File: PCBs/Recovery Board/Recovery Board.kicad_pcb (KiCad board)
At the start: 2 copper layers, 84.3 x 50.8 mm, 30 parts, among them J1 Conn_01x02, J2 Conn_01x02, J3 Conn_01x02, J4 Conn_01x02, J5 Conn_01x02, J6 Conn_01x02, U1 R-78E3.3-0.5, U2 PI4ULS5V201TAEX, U3 PI4ULS5V201TAEX, X1 XBee-S2C

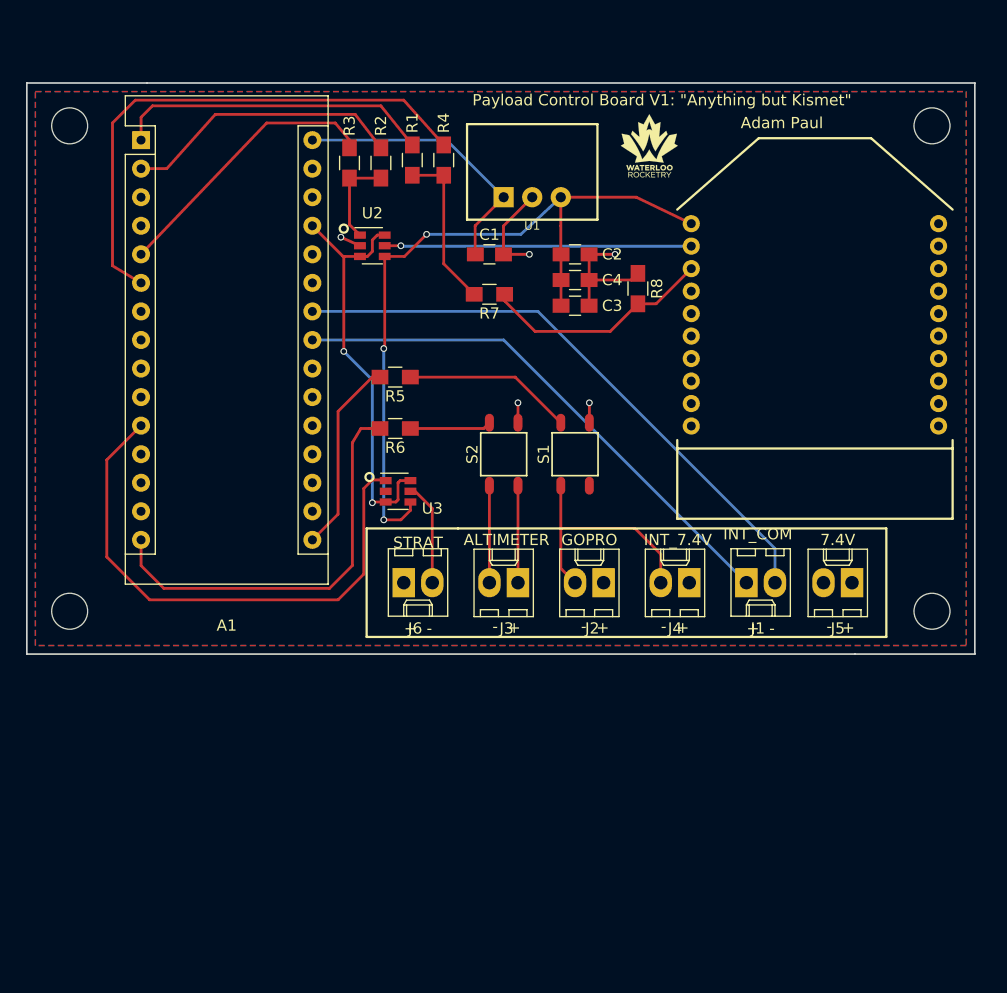
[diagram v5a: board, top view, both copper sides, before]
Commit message: swapped all mounting holes with plated ones, fixed disconnected components on recovery, added the 4 decoupling caps to recovery, fixed silk screen on pads in instr, fixed traces connecting through pads on recovery and instr, moved q1 on instr, brought trace in near u2 on instr, switched u2 & u3 to hand solder on instr, fixed xbee screen on recovery, fixed connector labels on recovery, removed recovery dims past edge cuts, fixed pad mask clearance on recovery
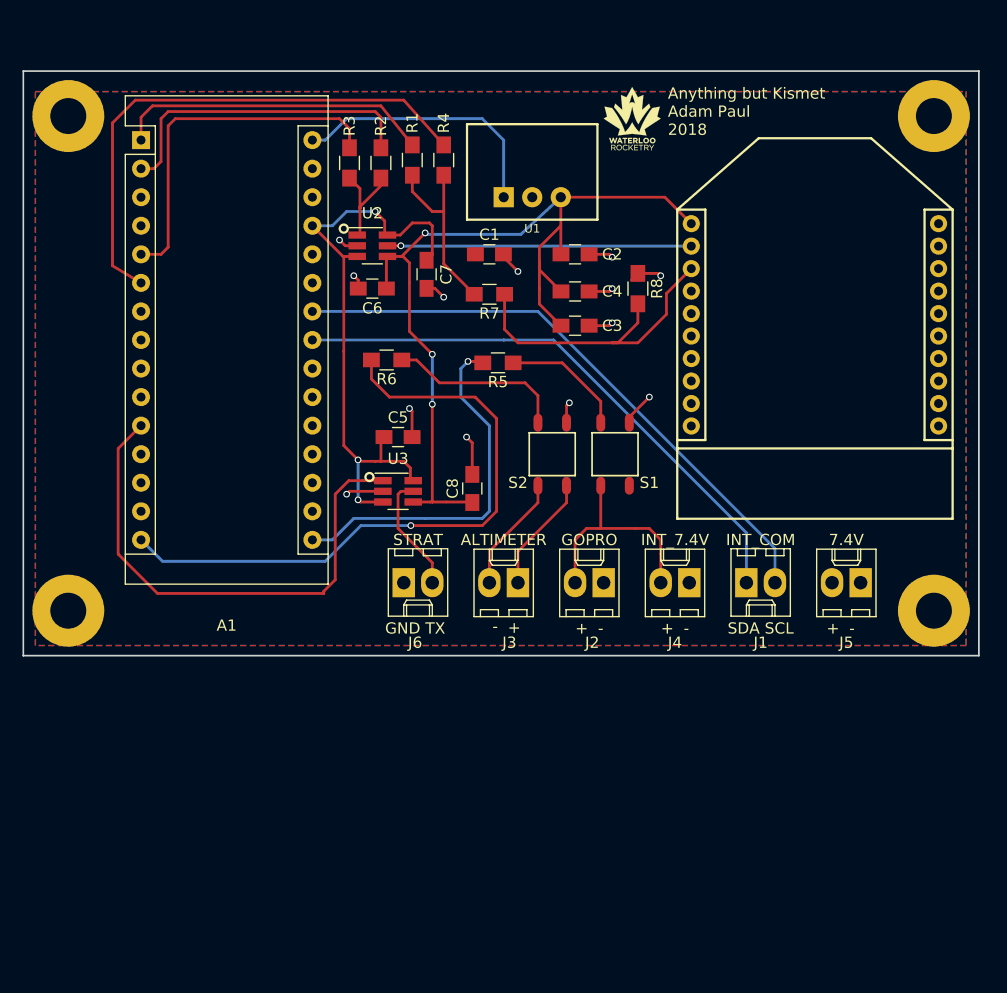
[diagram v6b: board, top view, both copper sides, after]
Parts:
- removed the REF** at (163.8, 146.1)
- removed the REF** at (87.1, 102.9)
- removed the REF** at (87.1, 146.1)
- added C5: 0.1uF, Capacitors_SMD:C_0805_HandSoldering, F.Cu at (116.3, 130.6)
- added C6: 0.1uF, Capacitors_SMD:C_0805_HandSoldering, F.Cu at (114.0, 117.3)
- added C7: 0.1uF, Capacitors_SMD:C_0805_HandSoldering, F.Cu at (118.9, 116.1)
- added C8: 0.1uF, Capacitors_SMD:C_0805_HandSoldering, F.Cu at (122.9, 135.1)
- added REF**: MountingHole_3.2mm_M3, Mounting_Holes:MountingHole_3.2mm_M3_Pad, F.Cu at (87.0, 102.0)
- added REF**: MountingHole_3.2mm_M3, Mounting_Holes:MountingHole_3.2mm_M3_Pad, F.Cu at (87.0, 146.0)
- added REF**: MountingHole_3.2mm_M3, Mounting_Holes:MountingHole_3.2mm_M3_Pad, F.Cu at (164.0, 146.0)
- REF**: footprint Mounting_Holes:MountingHole_3.2mm_M3 -> Mounting_Holes:MountingHole_3.2mm_M3_Pad
- U2, U3: value PI4ULS5V201TAEX -> PI4ULS5V201TAEX-RESCUE-instrumentation_board; footprint sot:SOT-23-6 -> TO_SOT_Packages_SMD:SOT-23-6_Handsoldering
- moved R5 9.23 mm to (125.2, 124.0)
- moved R6 6.14 mm to (115.3, 123.7)
- moved S2 4.32 mm to (130.0, 132.1)
- moved S1 3.56 mm to (135.6, 132.1)
- moved G*** 2.85 mm to (137.2, 102.2)
- moved C3 1.78 mm to (132.1, 120.7)
- moved C4 1.02 mm to (132.1, 117.6)
- moved REF** 0.89 mm to (164.0, 102.0)
- moved J5 0.76 mm to (157.5, 143.5)
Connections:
- J3 pad 1: Stratologger_Switch- -> Stratologger_Switch+
- J3 pad 2: Stratologger_Switch+ -> Stratologger_Switch-
- S2 pad 3: Stratologger_Switch+ -> Stratologger_Switch-
- S2 pad 4: Stratologger_Switch- -> Stratologger_Switch+
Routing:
- net Stratologger_Relay: track 36.9 -> 56.8 mm, vias 0 -> 1
- net 5V: track 37.0 -> 54.6 mm, vias 2 -> 3
- net Instr_Arduino_Relay: track 17.4 -> 32.8 mm, vias 0 -> 1
- net 3.3V: track 66.5 -> 80.8 mm
- net Net-(R7-Pad1): track 20.6 -> 29.4 mm
- net Net-(R6-Pad1): track 7.24 -> 15.8 mm
- net Net-(A1-Pad5): track 24.9 -> 32.6 mm
- net GND: track 25.3 -> 31.1 mm, vias 5 -> 13
- net Net-(R5-Pad1): track 15.1 -> 11.1 mm
- net Net-(A1-Pad2): track 25.0 -> 28.6 mm
- net SDA: track 47.6 -> 50.2 mm
- net XBEE-DIN: track 14.5 -> 16.7 mm
- net Stratologger_TX: track 9.18 -> 11.0 mm
- net Stratologger_Switch+: track 8.63 -> 10.4 mm
- net Stratologger_Switch-: track 8.63 -> 10.4 mm
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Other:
- board size 84.3 x 50.8 mm -> 85 x 52 mm
- rule pad_to_mask_clearance: 0.2 -> 0.05
- board text added: "Anything but Kismet Adam Paul 2018"
- board text added: "GND TX"
- board text added: "SDA SCL"
- board text removed: "Adam Paul"
- board text removed: "Payload Control Board V1: "Anything but Kismet""

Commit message: Changed connectors for recovery board batteries
Added a second connector for the other battery
Moved connectors to top of board
Replaced footprint with JST-PH
Extended board width
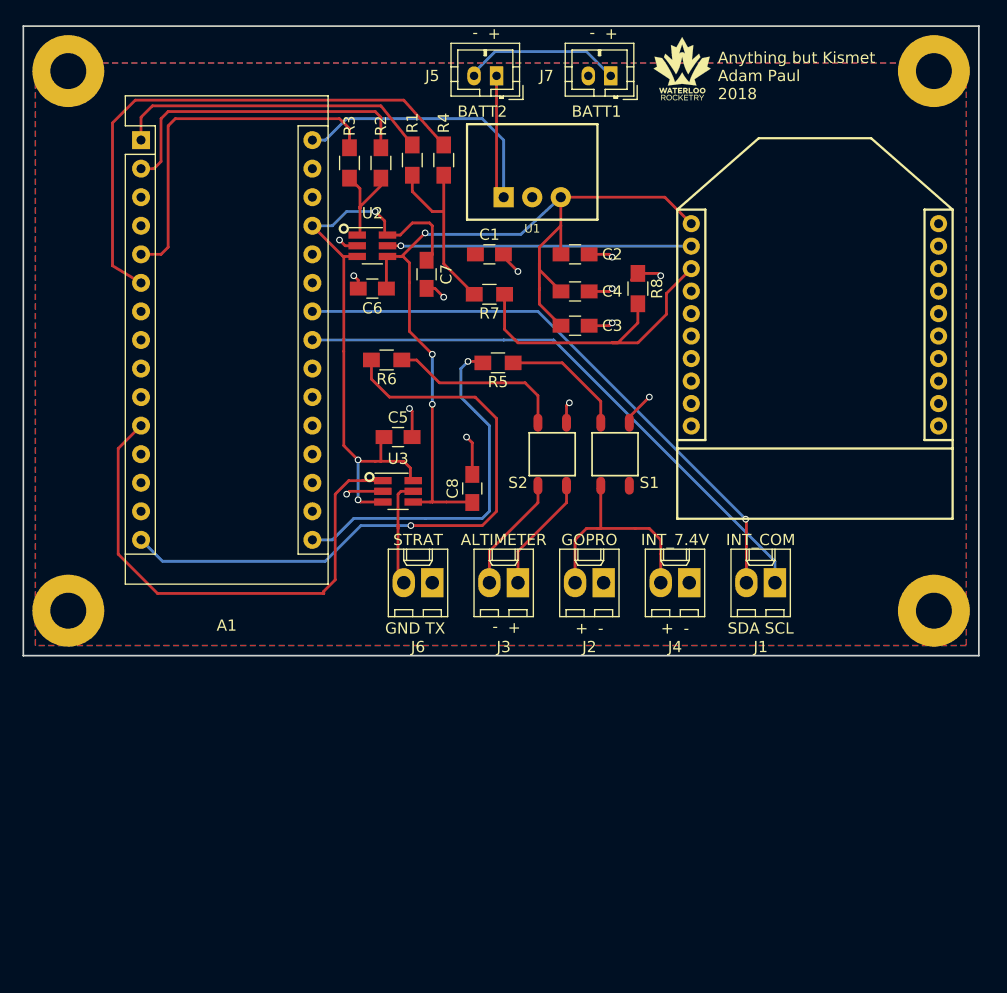
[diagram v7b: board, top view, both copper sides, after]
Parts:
- added J7: Conn_01x02, Connectors_JST:JST_PH_B2B-PH-K_02x2.00mm_Straight, F.Cu at (135.3, 98.4)
- J5: footprint Connectors_Molex:Molex_KK-6410-02_02x2.54mm_Straight -> Connectors_JST:JST_PH_B2B-PH-K_02x2.00mm_Straight
- moved J5 55.5 mm to (125.1, 98.4)
- moved G*** 6.29 mm to (141.6, 97.8)
- moved REF** 4.00 mm to (87.0, 98.0)
- moved REF** 4.00 mm to (164.0, 98.0)
- moved J1 2.54 mm to (149.9, 143.5), turned to 180 degrees
- moved J6 2.54 mm to (119.4, 143.5), turned to 180 degrees
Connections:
- J5 pad 1: GND -> 7.4V
- J5 pad 2: 7.4V -> Net-(J5-Pad2)
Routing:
- net Net-(J5-Pad2): track 0.00 -> 14.1 mm
- net 7.4V: track 23.7 -> 34.7 mm
- net SDA: track 50.2 -> 51.2 mm
- net SCL: track 52.9 -> 51.9 mm, vias 0 -> 1
- net Stratologger_TX: track 11.0 -> 10.2 mm
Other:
- board size 85 x 52 mm -> 85 x 56 mm
- board text added: "BATT1"
- board text added: "BATT2"
- board text removed: "7.4V"
